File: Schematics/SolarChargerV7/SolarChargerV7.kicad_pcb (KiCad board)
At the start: 2 copper layers, 74.5 x 47.6 mm, 24 parts, among them J1 USB_A, Q1 CSD16410Q5A, U1 LM3478MA_NOPB

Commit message: Version 7 final changes
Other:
- board size 74.5 x 47.6 mm -> 74.5 x 38.1 mm
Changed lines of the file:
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@@
       (sketchpadsonfab false)
       (subtractmaskfromsilk false)
-      (outputformat 4)
+      (outputformat 1)
       (mirror false)
       (drillshape 0)
       (scaleselection 1)
-      (outputdirectory "PDFV7/")
+      (outputdirectory "DrillV7/")
     )
   )
@@
     )
   )
-  (gr_rect (start 168 91.8) (end 93.5 44.2) (layer "Edge.Cuts") (width 0.1) (fill none))
-  (gr_text "Solar Powered 5V Phone Charger" (at 107.7 46.8) (layer "F.SilkS")
+  (gr_rect (start 168 86.08) (end 93.5 48) (layer "Edge.Cuts") (width 0.1) (fill none))
+  (gr_text "Solar Powered 5V Phone Charger" (at 150.51 49.44) (layer "F.SilkS")
     (effects (font (size 1 1) (thickness 0.15)))
   )
-  (gr_text "Joshua Mularczyk\nChristian Williams\nENGR 460 - Power Electronics" (at 165.735 86.995) (layer "F.SilkS")
+  (gr_text "Joshua Mularczyk\nChristian Williams\nENGR 460 - Power Electronics" (at 166.53 82.99) (layer "F.SilkS")
     (effects (font (size 0.9 0.9) (thickness 0.125)) (justify right))
   )
@@
     (polygon
       (pts
-        (xy 167.8 91.7)
-        (xy 93.5 91.7)
-        (xy 93.6 44.3)
-        (xy 168 44.1)
+        (xy 167.8 86.01)
+        (xy 93.5 86.01)
+        (xy 93.610299 48.131155)
+        (xy 168.010299 47.931155)
       )
     )

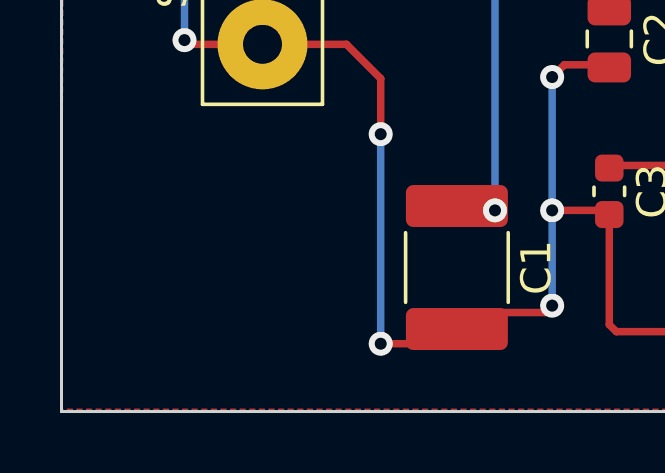
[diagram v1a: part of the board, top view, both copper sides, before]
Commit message: quick fix of resistor values for voltage divider
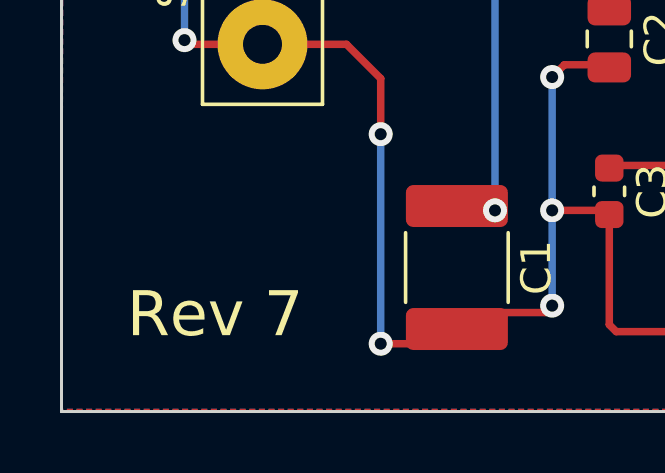
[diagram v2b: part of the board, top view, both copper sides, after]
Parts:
- R10: value 130k -> 150k
- R11: value 160k -> 100k
- R8: value 150k -> 130k
- R9: value 100k -> 160k
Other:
- board text added: "Rev 7"
